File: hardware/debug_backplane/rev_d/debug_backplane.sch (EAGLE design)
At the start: 324 parts, among them J1 BACKPLANE_CONTROLLER_MODULE_D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, J2 BACKPLANE_GENERIC_MODULE_DEBUG, J3 BACKPLANE_GENERIC_MODULE_DEBUG, J4 MICRO_USB_B_HIROSE_ZX62R-B-5P, J5 MICRO_USB_B_HIROSE_ZX62R-B-5P, J7 PJ-102AH, J8 TC2030-FTDI-I2C, Q1 DMN32D2LDF, Q2 DMN32D2LDF, Q3 DMN32D2LDF, Q4 DMN32D2LDF, Q5 DMN32D2LDF, Q6 DMN32D2LDF, Q7 DMN32D2LDF, Q8 MOSFET-NCHANNELSMD, U1 FT232RQ, U10 LTC2943, U11 LTC2943, U12 LTC2943, U13 LTC4360, U14 M24C01WMN, U15 MAX6746, U16 MAX8887EZK33+T, U17 MCP23008QFN, U18 MCP23008QFN, U19 MCP23008QFN, U2 FT232RQ, U20 NCP301LSN30, U21 NCP301LSN30, U22 PCA9544AQFN-N20, U23 SAM4LC8AA, U24 SN74LVC2T45, U25 SN74LVC2T45, U26 SN74LVC2T45, U27 SN74LVC2T45, U28 TS3USB30E, U29 TS3USB30E, U3 FT232RQ, U30 TS3USB30E, U31 TUSB2077A, U32 TUSB2077A, U4 FT232RQ, U5 FT232RQ, U6 FT232RQ, U7 FXMA2102, U8 FXMA2102, U9 LTC2941, Y1 ABMM, Y2 ABMM, Y3 FH1600015

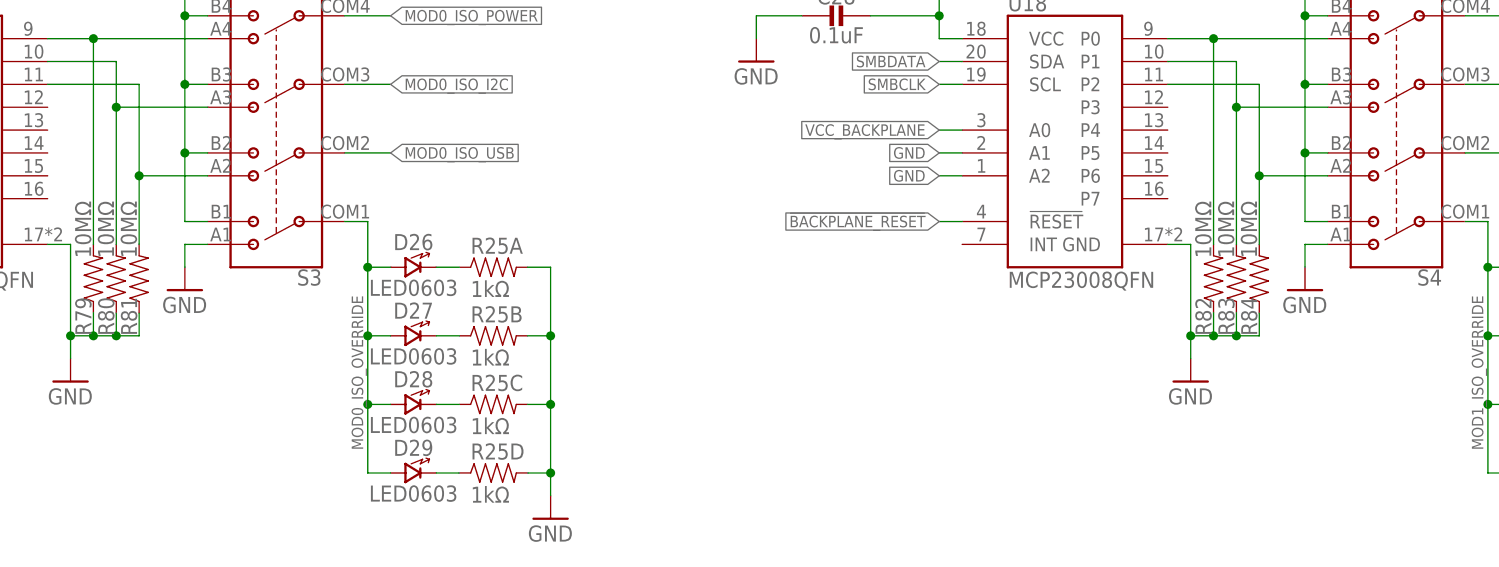
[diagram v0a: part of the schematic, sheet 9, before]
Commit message: debug_backplane: remove GND from iso switches
The isolation override switches have a momentary short when thrown.
For the LED control, this was shorting 3v3_unmetered to gnd. Just
let the LEDs float when they're off; no need to ground them.
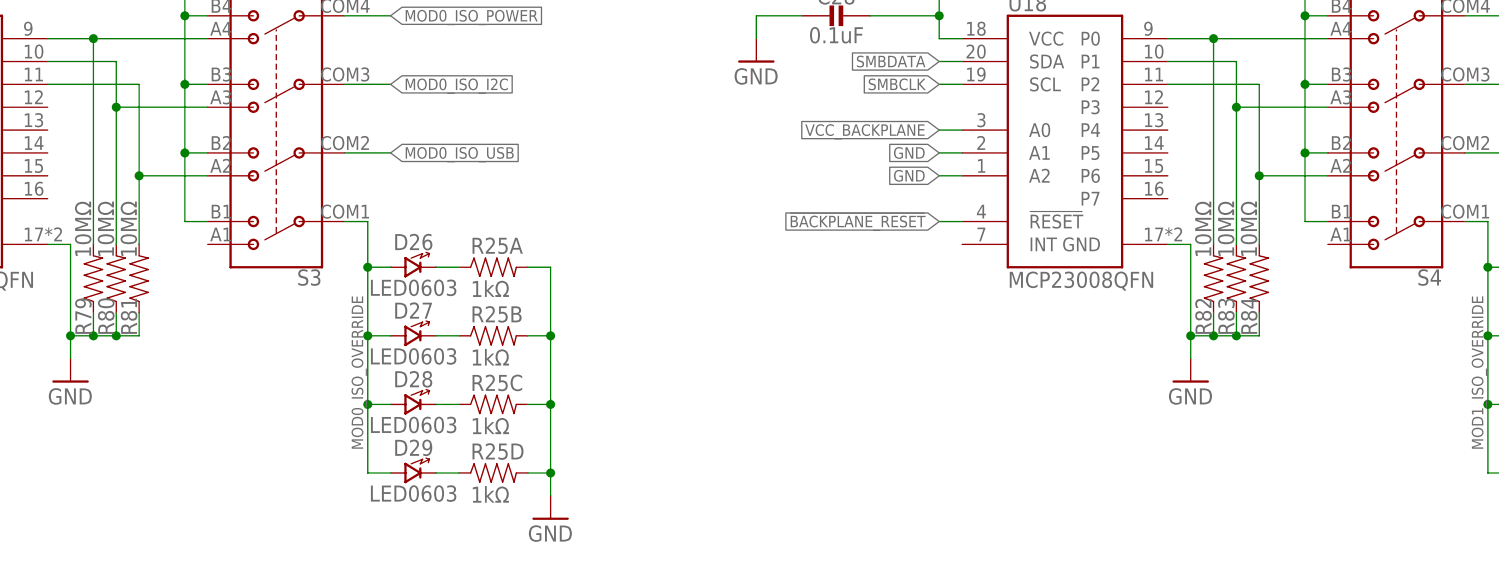
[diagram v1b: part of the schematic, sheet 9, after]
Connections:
- net GND: no longer S3.1TA, S4.1TA
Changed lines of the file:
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@@
 <part name="GND113" library="umich" deviceset="GND" device=""/>
 <part name="GND114" library="umich" deviceset="GND" device=""/>
-<part name="GND115" library="umich" deviceset="GND" device=""/>
 <part name="GND116" library="umich" deviceset="GND" device=""/>
 <part name="GND117" library="umich" deviceset="GND" device=""/>
@@
 <part name="GND11" library="umich" deviceset="GND" device=""/>
 <part name="GND120" library="umich" deviceset="GND" device=""/>
-<part name="GND121" library="umich" deviceset="GND" device=""/>
 <part name="GND122" library="umich" deviceset="GND" device=""/>
 <part name="GND123" library="umich" deviceset="GND" device=""/>
@@
 <instance part="GND110" gate="1" x="15.24" y="121.92"/>
 <instance part="GND113" gate="1" x="139.7" y="121.92"/>
-<instance part="GND115" gate="1" x="76.2" y="96.52"/>
 <instance part="GND120" gate="1" x="116.84" y="71.12"/>
-<instance part="GND121" gate="1" x="200.66" y="96.52"/>
 <instance part="GND122" gate="1" x="243.84" y="71.12"/>
 <instance part="GND64" gate="1" x="63.5" y="86.36"/>
@@
 </segment>
 <segment>
-<pinref part="GND115" gate="1" pin="GND"/>
-<pinref part="S3" gate="G$1" pin="1TA"/>
-<wire x1="76.2" y1="101.6" x2="76.2" y2="99.06" width="0.1524" layer="91"/>
-<wire x1="78.74" y1="101.6" x2="76.2" y2="101.6" width="0.1524" layer="91"/>
-</segment>
-<segment>
 <pinref part="GND120" gate="1" pin="GND"/>
 <pinref part="R25" gate="A" pin="2"/>
@@
 </segment>
 <segment>
-<pinref part="GND121" gate="1" pin="GND"/>
-<pinref part="S4" gate="G$1" pin="1TA"/>
-<wire x1="200.66" y1="101.6" x2="200.66" y2="99.06" width="0.1524" layer="91"/>
-<wire x1="203.2" y1="101.6" x2="200.66" y2="101.6" width="0.1524" layer="91"/>
-</segment>
-<segment>

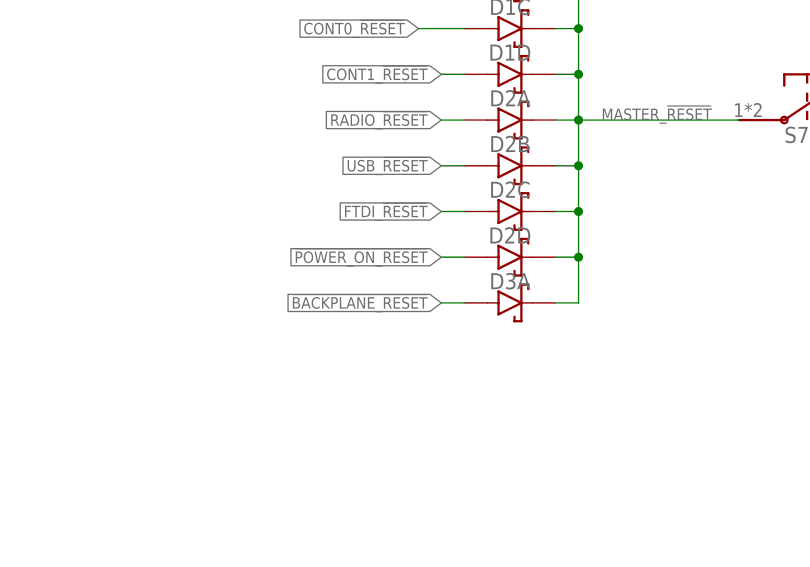
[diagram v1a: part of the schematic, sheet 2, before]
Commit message: debug_backplane: don't reset debug usb hub
If you want to reset this, you can pretty much just pull the plug
on the board
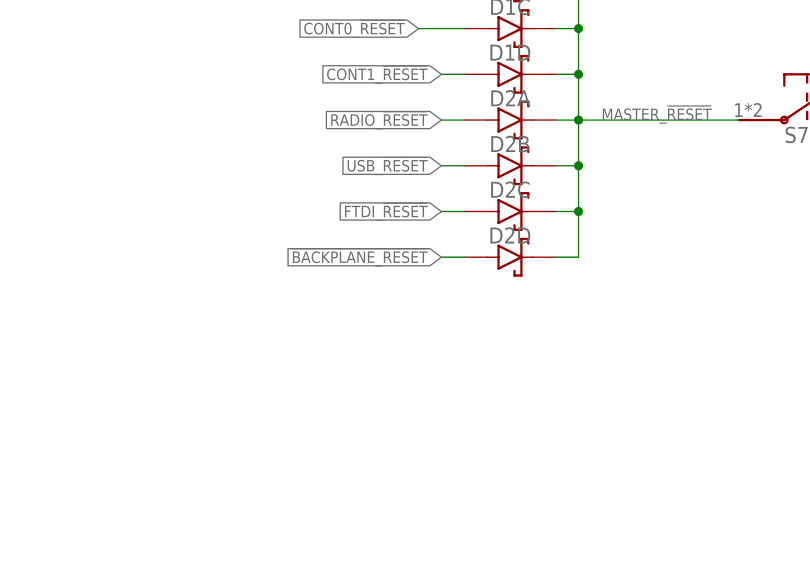
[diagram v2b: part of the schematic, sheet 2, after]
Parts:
- removed D3: DIODE_SCHOTTKY_ARRAY-4HMD8, passives:DIODE_SCHOTTKY_ARRAY-4HMD8
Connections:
- net !BACKPLANE_RESET: now also D2D.ANODE; no longer D3A.ANODE
- net !POWER_ON_RESET: no longer D2D.ANODE
- net MASTER_!RESET: no longer D3A.CATHODE
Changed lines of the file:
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@@
 <part name="D35" library="signpost" deviceset="SN75240-TSSOP" device=""/>
 <part name="D36" library="signpost" deviceset="SN75240-TSSOP" device=""/>
-<part name="D3" library="passives" deviceset="DIODE_SCHOTTKY_ARRAY-4" device="HMD8"/>
 <part name="D4" library="leds" deviceset="LED" device="0603">
 <attribute name="DESCRIPTION" value="LED GREEN CLEAR 0603 SMD"/>
@@
 <attribute name="DIGIKEY" x="170.18" y="170.18" size="1.016" layer="96" rot="R270" align="bottom-center" display="off"/>
 </instance>
-<instance part="D3" gate="A" x="109.22" y="43.18"/>
 <instance part="FRAME18" gate="G$1" x="0" y="0"/>
 <instance part="FRAME18" gate="G$2" x="152.4" y="0"/>
@@
 <net name="!BACKPLANE_RESET" class="0">
 <segment>
-<pinref part="D3" gate="A" pin="ANODE"/>
-<wire x1="101.6" y1="43.18" x2="104.14" y2="43.18" width="0.1524" layer="91"/>
-<label x="101.6" y="43.18" size="1.27" layer="95" rot="R180" xref="yes"/>
-</segment>
-</net>
-<net name="!POWER_ON_RESET" class="0">
-<segment>
+<label x="101.6" y="48.26" size="1.27" layer="95" rot="R180" xref="yes"/>
 <pinref part="D2" gate="D" pin="ANODE"/>
 <wire x1="101.6" y1="48.26" x2="104.14" y2="48.26" width="0.1524" layer="91"/>
-<label x="101.6" y="48.26" size="1.27" layer="95" rot="R180" xref="yes"/>
 </segment>
 </net>
@@
 <pinref part="D2" gate="C" pin="CATHODE"/>
 <pinref part="D2" gate="D" pin="CATHODE"/>
-<pinref part="D3" gate="A" pin="CATHODE"/>
 <pinref part="S7" gate="G$1" pin="P$1"/>
-<wire x1="114.3" y1="43.18" x2="116.84" y2="43.18" width="0.1524" layer="91"/>
 <wire x1="114.3" y1="48.26" x2="116.84" y2="48.26" width="0.1524" layer="91"/>
 <wire x1="114.3" y1="53.34" x2="116.84" y2="53.34" width="0.1524" layer="91"/>
@@
 <wire x1="114.3" y1="78.74" x2="116.84" y2="78.74" width="0.1524" layer="91"/>
 <wire x1="114.3" y1="83.82" x2="116.84" y2="83.82" width="0.1524" layer="91"/>
-<wire x1="116.84" y1="43.18" x2="116.84" y2="48.26" width="0.1524" layer="91"/>
 <wire x1="116.84" y1="48.26" x2="116.84" y2="53.34" width="0.1524" layer="91"/>
 <wire x1="116.84" y1="53.34" x2="116.84" y2="58.42" width="0.1524" layer="91"/>
@@
 <wire x1="116.84" y1="83.82" x2="116.84" y2="78.74" width="0.1524" layer="91"/>
 <wire x1="134.62" y1="63.5" x2="116.84" y2="63.5" width="0.1524" layer="91"/>
-<junction x="116.84" y="48.26"/>
 <junction x="116.84" y="53.34"/>
 <junction x="116.84" y="58.42"/>

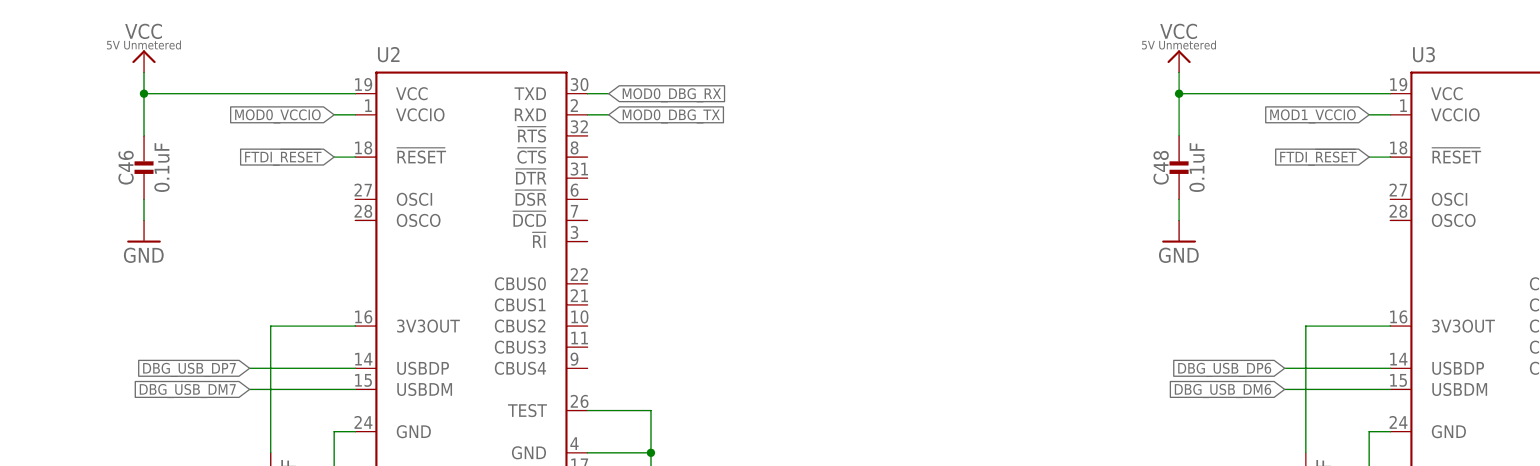
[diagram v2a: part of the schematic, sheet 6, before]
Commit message: debug_backplane: don't reset FTDIs either
follows the same logic as the last commit
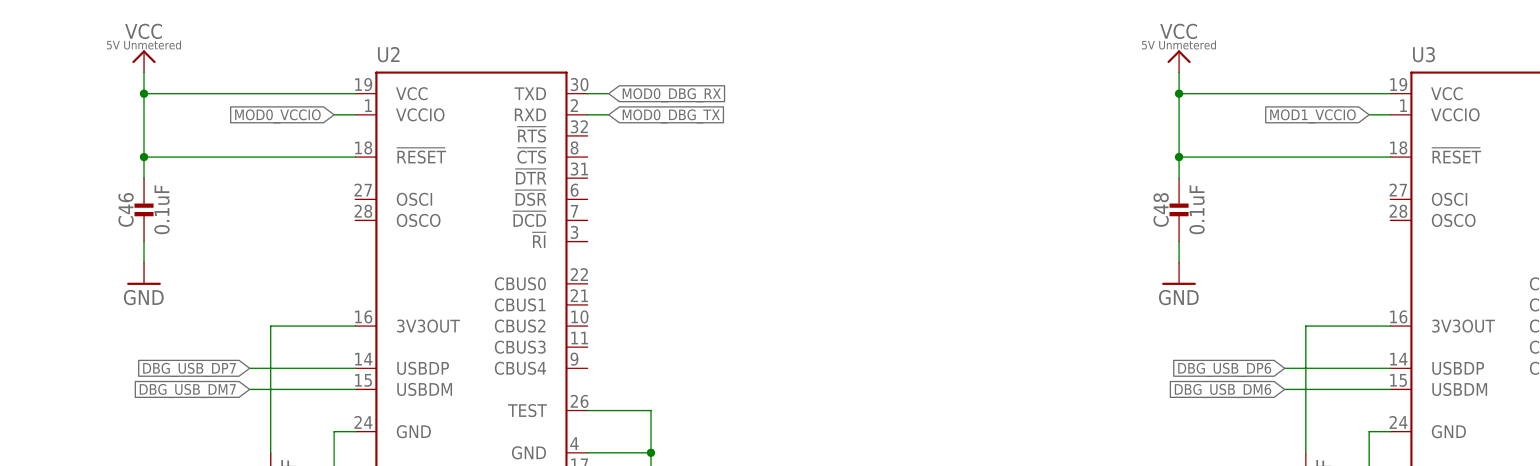
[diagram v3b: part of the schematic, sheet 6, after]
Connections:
- removed net FTDI_!RESET: D2C.ANODE, U1.!RESET, U2.!RESET, U3.!RESET, U4.!RESET, U5.!RESET, U6.!RESET
- net 5V_UNMETERED: now also U1.!RESET, U2.!RESET, U3.!RESET, U4.!RESET, U5.!RESET, U6.!RESET
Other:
- moved on the sheet: C46, C48
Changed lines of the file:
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@@
 </segment>
 </net>
-<net name="FTDI_!RESET" class="0">
-<segment>
-<pinref part="D2" gate="C" pin="ANODE"/>
-<wire x1="101.6" y1="53.34" x2="104.14" y2="53.34" width="0.1524" layer="91"/>
-<label x="101.6" y="53.34" size="1.27" layer="95" rot="R180" xref="yes"/>
-</segment>
-</net>
 <net name="GND" class="0">
 <segment>
@@
 <instances>
 <instance part="C45" gate="G$1" x="45.72" y="116.84"/>
-<instance part="C46" gate="G$1" x="30.48" y="154.94"/>
+<instance part="C46" gate="G$1" x="30.48" y="149.86"/>
 <instance part="C47" gate="G$1" x="170.18" y="116.84"/>
-<instance part="C48" gate="G$1" x="154.94" y="154.94"/>
+<instance part="C48" gate="G$1" x="154.94" y="149.86"/>
 <instance part="D10" gate="G$1" x="76.2" y="78.74" rot="R270">
 <attribute name="DIGIKEY" x="76.2" y="78.74" size="1.016" layer="96" rot="R270" align="bottom-center" display="off"/>
@@
 <instance part="GND33" gate="1" x="45.72" y="106.68"/>
 <instance part="GND50" gate="1" x="53.34" y="106.68"/>
-<instance part="GND51" gate="1" x="30.48" y="144.78"/>
+<instance part="GND51" gate="1" x="30.48" y="139.7"/>
 <instance part="GND52" gate="1" x="177.8" y="106.68"/>
 <instance part="GND53" gate="1" x="91.44" y="106.68"/>
 <instance part="GND54" gate="1" x="170.18" y="106.68"/>
-<instance part="GND60" gate="1" x="154.94" y="144.78"/>
+<instance part="GND60" gate="1" x="154.94" y="139.7"/>
 <instance part="GND62" gate="1" x="215.9" y="106.68"/>
 <instance part="GND90" gate="1" x="53.34" y="27.94"/>
@@
 <pinref part="U$31" gate="G$1" pin="5V_UNMETERED"/>
 <pinref part="U2" gate="1" pin="VCC"/>
-<wire x1="30.48" y1="157.48" x2="30.48" y2="162.56" width="0.1524" layer="91"/>
+<wire x1="30.48" y1="152.4" x2="30.48" y2="154.94" width="0.1524" layer="91"/>
+<wire x1="30.48" y1="154.94" x2="30.48" y2="162.56" width="0.1524" layer="91"/>
 <wire x1="30.48" y1="162.56" x2="30.48" y2="165.1" width="0.1524" layer="91"/>
 <wire x1="30.48" y1="162.56" x2="55.88" y2="162.56" width="0.1524" layer="91"/>
 <junction x="30.48" y="162.56"/>
+<pinref part="U2" gate="1" pin="!RESET"/>
+<wire x1="55.88" y1="154.94" x2="30.48" y2="154.94" width="0.1524" layer="91"/>
+<junction x="30.48" y="154.94"/>
 </segment>
 <segment>
@@
 <pinref part="U$34" gate="G$1" pin="5V_UNMETERED"/>
 <pinref part="U3" gate="1" pin="VCC"/>
-<wire x1="154.94" y1="157.48" x2="154.94" y2="162.56" width="0.1524" layer="91"/>
+<wire x1="154.94" y1="152.4" x2="154.94" y2="154.94" width="0.1524" layer="91"/>
+<wire x1="154.94" y1="154.94" x2="154.94" y2="162.56" width="0.1524" layer="91"/>
 <wire x1="154.94" y1="162.56" x2="180.34" y2="162.56" width="0.1524" layer="91"/>
 <wire x1="154.94" y1="165.1" x2="154.94" y2="162.56" width="0.1524" layer="91"/>
 <junction x="154.94" y="162.56"/>
+<pinref part="U3" gate="1" pin="!RESET"/>
+<wire x1="180.34" y1="154.94" x2="154.94" y2="154.94" width="0.1524" layer="91"/>
+<junction x="154.94" y="154.94"/>
 </segment>
 </net>
@@
 </segment>
 </net>
-<net name="FTDI_!RESET" class="0">
-<segment>
-<pinref part="U2" gate="1" pin="!RESET"/>
-<wire x1="53.34" y1="154.94" x2="55.88" y2="154.94" width="0.1524" layer="91"/>
-<label x="53.34" y="154.94" size="1.27" layer="95" rot="R180" xref="yes"/>
-</segment>
-<segment>
-<pinref part="U3" gate="1" pin="!RESET"/>
-<wire x1="177.8" y1="154.94" x2="180.34" y2="154.94" width="0.1524" layer="91"/>
-<label x="177.8" y="154.94" size="1.27" layer="95" rot="R180" xref="yes"/>
-</segment>
-</net>
 <net name="GND" class="0">
 <segment>
 <pinref part="C46" gate="G$1" pin="2"/>
 <pinref part="GND51" gate="1" pin="GND"/>
-<wire x1="30.48" y1="149.86" x2="30.48" y2="147.32" width="0.1524" layer="91"/>
+<wire x1="30.48" y1="144.78" x2="30.48" y2="142.24" width="0.1524" layer="91"/>
 </segment>
 <segment>
@@
 <pinref part="C48" gate="G$1" pin="2"/>
 <pinref part="GND60" gate="1" pin="GND"/>
-<wire x1="154.94" y1="149.86" x2="154.94" y2="147.32" width="0.1524" layer="91"/>
+<wire x1="154.94" y1="144.78" x2="154.94" y2="142.24" width="0.1524" layer="91"/>
 </segment>
 <segment>
@@
 <wire x1="53.34" y1="121.92" x2="53.34" y2="165.1" width="0.1524" layer="91"/>
 <wire x1="53.34" y1="165.1" x2="50.8" y2="165.1" width="0.1524" layer="91"/>
-<wire x1="53.34" y1="165.1" x2="73.66" y2="165.1" width="0.1524" layer="91"/>
+<wire x1="53.34" y1="165.1" x2="71.12" y2="165.1" width="0.1524" layer="91"/>
 <junction x="53.34" y="165.1"/>
+<pinref part="U4" gate="1" pin="!RESET"/>
+<wire x1="71.12" y1="165.1" x2="73.66" y2="165.1" width="0.1524" layer="91"/>
+<wire x1="73.66" y1="157.48" x2="71.12" y2="157.48" width="0.1524" layer="91"/>
+<wire x1="71.12" y1="157.48" x2="71.12" y2="165.1" width="0.1524" layer="91"/>
+<junction x="71.12" y="165.1"/>
 </segment>
 <segment>
@@
 <wire x1="182.88" y1="121.92" x2="182.88" y2="165.1" width="0.1524" layer="91"/>
 <wire x1="182.88" y1="165.1" x2="180.34" y2="165.1" width="0.1524" layer="91"/>
-<wire x1="182.88" y1="165.1" x2="203.2" y2="165.1" width="0.1524" layer="91"/>
+<wire x1="182.88" y1="165.1" x2="200.66" y2="165.1" width="0.1524" layer="91"/>
 <junction x="182.88" y="165.1"/>
+<pinref part="U5" gate="1" pin="!RESET"/>
+<wire x1="200.66" y1="165.1" x2="203.2" y2="165.1" width="0.1524" layer="91"/>
+<wire x1="203.2" y1="157.48" x2="200.66" y2="157.48" width="0.1524" layer="91"/>
+<wire x1="200.66" y1="157.48" x2="200.66" y2="165.1" width="0.1524" layer="91"/>
+<junction x="200.66" y="165.1"/>
 </segment>
 </net>
@@
 </segment>
 </net>
-<net name="FTDI_!RESET" class="0">
-<segment>
-<pinref part="U4" gate="1" pin="!RESET"/>
-<wire x1="71.12" y1="157.48" x2="73.66" y2="157.48" width="0.1524" layer="91"/>
-<label x="71.12" y="157.48" size="1.27" layer="95" rot="R180" xref="yes"/>
-</segment>
-<segment>
-<pinref part="U5" gate="1" pin="!RESET"/>
-<wire x1="200.66" y1="157.48" x2="203.2" y2="157.48" width="0.1524" layer="91"/>
-<label x="200.66" y="157.48" size="1.27" layer="95" rot="R180" xref="yes"/>
-</segment>
-</net>
 <net name="GND" class="0">
 <segment>
@@
 <pinref part="U6" gate="1" pin="VCC"/>
 <wire x1="228.6" y1="40.64" x2="228.6" y2="81.28" width="0.1524" layer="91"/>
-<wire x1="228.6" y1="81.28" x2="205.74" y2="81.28" width="0.1524" layer="91"/>
+<wire x1="228.6" y1="81.28" x2="208.28" y2="81.28" width="0.1524" layer="91"/>
+<wire x1="208.28" y1="81.28" x2="205.74" y2="81.28" width="0.1524" layer="91"/>
 <wire x1="228.6" y1="81.28" x2="233.68" y2="81.28" width="0.1524" layer="91"/>
 <wire x1="233.68" y1="81.28" x2="233.68" y2="83.82" width="0.1524" layer="91"/>
 <junction x="228.6" y="81.28"/>
+<pinref part="U6" gate="1" pin="!RESET"/>
+<wire x1="205.74" y1="73.66" x2="208.28" y2="73.66" width="0.1524" layer="91"/>
+<wire x1="208.28" y1="73.66" x2="208.28" y2="81.28" width="0.1524" layer="91"/>
+<junction x="208.28" y="81.28"/>
 </segment>
 <segment>
@@
 <pinref part="U1" gate="1" pin="VCC"/>
 <wire x1="228.6" y1="109.22" x2="228.6" y2="149.86" width="0.1524" layer="91"/>
-<wire x1="228.6" y1="149.86" x2="205.74" y2="149.86" width="0.1524" layer="91"/>
+<wire x1="228.6" y1="149.86" x2="208.28" y2="149.86" width="0.1524" layer="91"/>
+<wire x1="208.28" y1="149.86" x2="205.74" y2="149.86" width="0.1524" layer="91"/>
 <wire x1="231.14" y1="149.86" x2="228.6" y2="149.86" width="0.1524" layer="91"/>
 <wire x1="231.14" y1="149.86" x2="231.14" y2="152.4" width="0.1524" layer="91"/>
 <junction x="228.6" y="149.86"/>
+<pinref part="U1" gate="1" pin="!RESET"/>
+<wire x1="205.74" y1="142.24" x2="208.28" y2="142.24" width="0.1524" layer="91"/>
+<wire x1="208.28" y1="142.24" x2="208.28" y2="149.86" width="0.1524" layer="91"/>
+<junction x="208.28" y="149.86"/>
 </segment>
 </net>
@@
 </segment>
 </net>
-<net name="FTDI_!RESET" class="0">
-<segment>
-<pinref part="U1" gate="1" pin="!RESET"/>
-<wire x1="208.28" y1="142.24" x2="205.74" y2="142.24" width="0.1524" layer="91"/>
-<label x="208.28" y="142.24" size="1.27" layer="95" xref="yes"/>
-</segment>
-<segment>
-<pinref part="U6" gate="1" pin="!RESET"/>
-<wire x1="208.28" y1="73.66" x2="205.74" y2="73.66" width="0.1524" layer="91"/>
-<label x="208.28" y="73.66" size="1.27" layer="95" xref="yes"/>
-</segment>
-</net>
